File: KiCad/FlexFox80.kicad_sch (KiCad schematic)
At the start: 29 parts, among them J101 DIN-5_180degree, J102 Conn_01x02, Q102 IRF610, U107 LM5134B

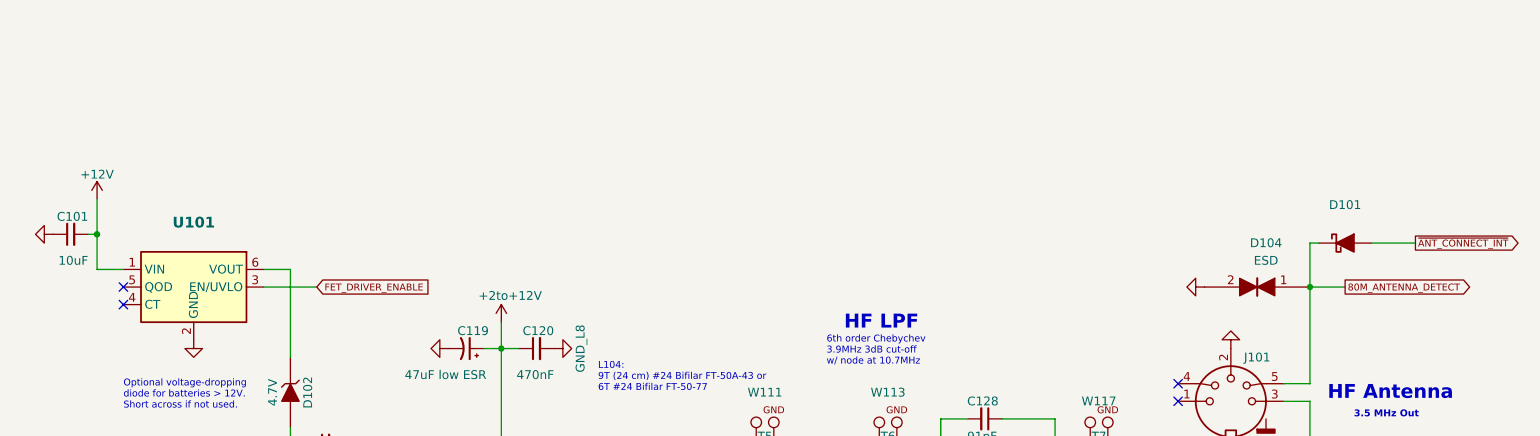
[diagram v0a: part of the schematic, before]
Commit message: KiCad Updates
o Fixes for problems found during first board build
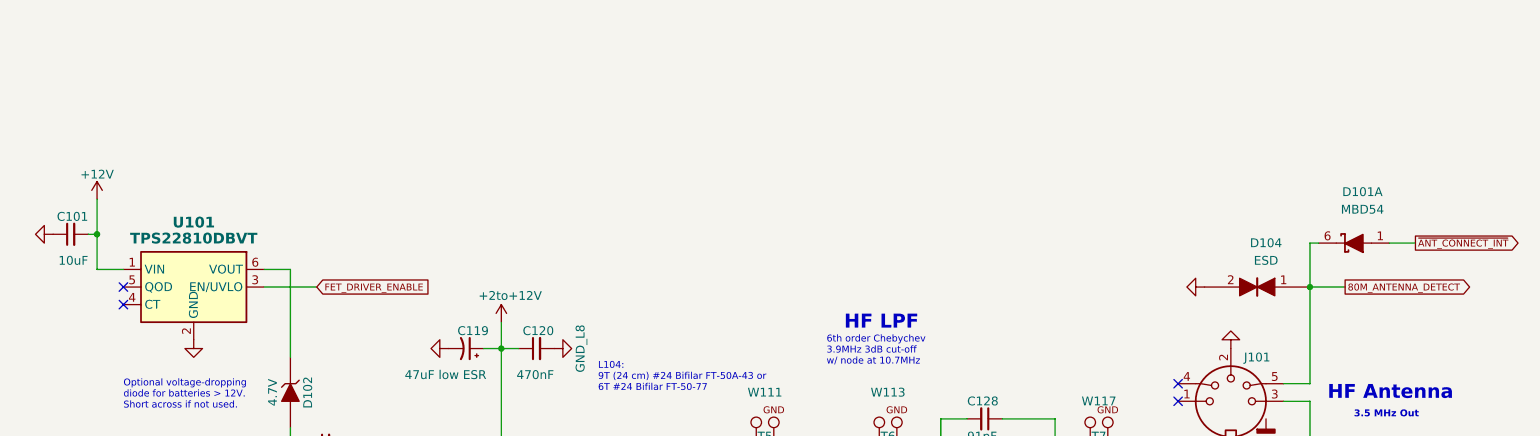
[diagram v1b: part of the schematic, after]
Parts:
- removed D101: MBD54, TO_SOT_Packages_SMD:SOT-363-0.65_MBD54, symbol FlexFox80-rescue:D_Schottky_ALT-Device
- added D101: MBD54DWT1G_Schottky_Ind-ARDF-2-Band-MiniTx-rescue, MBD54, symbol FlexFox80-rescue:MBD54DWT1G_Schottky_Ind-ARDF-2-Band-MiniTx-rescue
- U101: value (none) -> TPS22810DBVT; footprint (none) -> TO_SOT_Packages_SMD:SOT-23-6
- W105, W106, W108, W111, W113, W117: footprint Measurement_Points:Measurement_Point_ScopeProbe_Round-SMD-2sides-Pad_Small -> Measurement:Measurement_Point_ScopeProbe_Round-SMD-2sides-Pad_Small
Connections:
- net 80M_ANTENNA_DETECT: now also D101.6 (C)
- net ~{ANT_CONNECT_INT}: now also D101.1 (A)

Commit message: Updates
Schematic
Fixes to events.html
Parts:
- J102: value Conn_01x02 -> (none); footprint Pin_Headers:Pin_Header_Straight_1x02 -> (none)
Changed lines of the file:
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@@
     (in_bom yes) (on_board yes)
     (property "Reference" "J102" (id 0) (at 92.71 100.33 0))
-    (property "Value" "Conn_01x02" (id 1) (at 90.6272 99.4664 0)
-      (effects (font (size 1.27 1.27)) hide)
-    )
-    (property "Footprint" "Pin_Headers:Pin_Header_Straight_1x02" (id 2) (at 92.71 105.41 0)
+    (property "Value" "" (id 1) (at 90.6272 99.4664 0)
+      (effects (font (size 1.27 1.27)) hide)
+    )
+    (property "Footprint" "" (id 2) (at 92.71 105.41 0)
       (effects (font (size 1.27 1.27)) hide)
     )
@@
       (reference "#PWR0309") (unit 1) (value "GNDD") (footprint "")
     )
+    (path "/00000000-0000-0000-0000-00005bc7f38c/ae6aa4fd-de19-4521-8377-1280b62d121c"
+      (reference "#PWR?") (unit 1) (value "GNDD") (footprint "")
+    )
+    (path "/00000000-0000-0000-0000-0000591bc960/eed54263-4042-4250-b65b-f4823a51e154"
+      (reference "#PWR?") (unit 1) (value "GND_L8") (footprint "")
+    )
     (path "/00000000-0000-0000-0000-00005bf4c520/00000000-0000-0000-0000-00005bf4cc06"
       (reference "BOX401") (unit 1) (value "Chassis Box") (footprint "Oddities:Dummy_Empty")
@@
     )
     (path "/00000000-0000-0000-0000-000060a40aaa"
-      (reference "J102") (unit 1) (value "Conn_01x02") (footprint "Pin_Headers:Pin_Header_Straight_1x02")
+      (reference "J102") (unit 1) (value "Conn_01x02") (footprint "Connector_PinHeader_2.54mm:PinHeader_1x02_P2.54mm_Vertical")
     )
     (path "/00000000-0000-0000-0000-0000591bc960/00000000-0000-0000-0000-00005c64c637"
@@
     )
     (path "/00000000-0000-0000-0000-00005bc7f38c/00000000-0000-0000-0000-000060a04d07"
-      (reference "J302") (unit 1) (value "Conn_01x06") (footprint "Pin_Headers:Pin_Header_Angled_1x06")
+      (reference "J302") (unit 1) (value "Conn_01x06") (footprint "Connector_PinHeader_2.54mm:PinHeader_1x06_P2.54mm_Vertical")
     )
     (path "/00000000-0000-0000-0000-00005bc7f38c/00000000-0000-0000-0000-0000609fe9a1"
@@
     )
     (path "/00000000-0000-0000-0000-00005bc7f38c/00000000-0000-0000-0000-000061c4fe52"
-      (reference "J304") (unit 1) (value "Conn_01x10") (footprint "Pin_Headers:Pin_Header_Straight_1x10")
+      (reference "J304") (unit 1) (value "Conn_01x10") (footprint "Connector_PinHeader_2.54mm:PinHeader_1x10_P2.54mm_Vertical")
     )
     (path "/00000000-0000-0000-0000-00005bc7f38c/00000000-0000-0000-0000-000062a55759"
-      (reference "J305") (unit 1) (value "Conn_01x02") (footprint "Pin_Headers:Pin_Header_Straight_1x02")
+      (reference "J305") (unit 1) (value "Conn_01x02") (footprint "Connector_PinHeader_2.54mm:PinHeader_1x02_P2.54mm_Vertical")
     )
     (path "/00000000-0000-0000-0000-00005bc7f38c/00000000-0000-0000-0000-000062a34144"
-      (reference "J306") (unit 1) (value "Conn_01x02") (footprint "Pin_Headers:Pin_Header_Straight_1x02")
+      (reference "J306") (unit 1) (value "Conn_01x02") (footprint "Connector_PinHeader_2.54mm:PinHeader_1x02_P2.54mm_Vertical")
     )
     (path "/00000000-0000-0000-0000-00005bc7f38c/00000000-0000-0000-0000-000062a0f023"
-      (reference "J307") (unit 1) (value "Conn_01x02") (footprint "Pin_Headers:Pin_Header_Straight_1x02")
+      (reference "J307") (unit 1) (value "Conn_01x02") (footprint "Connector_PinHeader_2.54mm:PinHeader_1x02_P2.54mm_Vertical")
     )
     (path "/00000000-0000-0000-0000-00005bc7f38c/00000000-0000-0000-0000-00006208b0c7"
-      (reference "J308") (unit 1) (value "Conn_01x02") (footprint "Pin_Headers:Pin_Header_Straight_1x02")
+      (reference "J308") (unit 1) (value "Conn_01x03") (footprint "Connector_PinHeader_2.54mm:PinHeader_1x03_P2.54mm_Vertical")
     )
     (path "/00000000-0000-0000-0000-00005bf4c520/00000000-0000-0000-0000-00005c10b0e5"
@@
       (reference "J403") (unit 1) (value "CONN_01X10") (footprint "Oddities:Dummy_Empty")
     )
+    (path "/00000000-0000-0000-0000-0000591bc960/0d6d79aa-3153-425d-b3e8-bdf472b45573"
+      (reference "J?") (unit 1) (value "Conn_01x02") (footprint "Connector_PinHeader_2.54mm:PinHeader_1x02_P2.54mm_Vertical")
+    )
     (path "/00000000-0000-0000-0000-0000591bc960/00000000-0000-0000-0000-000062207d51"
       (reference "JP201") (unit 1) (value "Boost Bypass") (footprint "Wire_Connections_Bridges:Solder-Jumper-NO-SMD-Pad_Small")
@@
       (reference "JP301") (unit 1) (value "Jumper_NO_Small") (footprint "Wire_Connections_Bridges:Solder-Jumper-NO-SMD-Pad_Small")
     )
+    (path "/00000000-0000-0000-0000-00005bc7f38c/290392e3-0d5b-4ead-b60f-8e77273ebc5a"
+      (reference "JP?") (unit 1) (value "Jumper_NO_Small") (footprint "Wire_Connections_Bridges:Solder-Jumper-NO-SMD-Pad_Small")
+    )
     (path "/00000000-0000-0000-0000-00005cb66258"
       (reference "L104") (unit 1) (value "9T #24 Bifilar T50-43") (footprint "Inductors:Toroid_T-50A_TH_BF_CT_Vertical")
@@
     )
     (path "/00000000-0000-0000-0000-00005bc7f38c/00000000-0000-0000-0000-00005bcbb8a3"
-      (reference "P304") (unit 1) (value "Header") (footprint "Pin_Headers:Pin_Header_Straight_1x06")
+      (reference "P304") (unit 1) (value "Header") (footprint "Connector_PinHeader_2.54mm:PinHeader_1x06_P2.54mm_Vertical")
     )
     (path "/00000000-0000-0000-0000-00005bf4c520/00000000-0000-0000-0000-00005bf5c2d3"
@@
     )
     (path "/00000000-0000-0000-0000-00005bc7f38c/00000000-0000-0000-0000-000061c41f8a"
-      (reference "TP301") (unit 1) (value "I2C1") (footprint "Pin_Headers:Pin_Header_Straight_1x04")
+      (reference "TP301") (unit 1) (value "I2C1") (footprint "Connector_PinHeader_2.54mm:PinHeader_1x04_P2.54mm_Vertical")
     )
     (path "/00000000-0000-0000-0000-00005bc7f38c/00000000-0000-0000-0000-0000608ada8e"
-      (reference "TP302") (unit 1) (value "I2C0") (footprint "Pin_Headers:Pin_Header_Straight_1x04")
+      (reference "TP302") (unit 1) (value "I2C0") (footprint "Connector_PinHeader_2.54mm:PinHeader_1x04_P2.54mm_Vertical")
     )
     (path "/00000000-0000-0000-0000-0000628d7f12"
